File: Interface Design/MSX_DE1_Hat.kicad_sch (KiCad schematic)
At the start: 24 parts, among them J1 J1, J2 J2, J3 J3, J4 J4, J5 J5, J6 J6, U1 74LVC245A, U2 74LVC245A, U3 74LVC245A, U4 74LVC245A, U5 74LVC245A

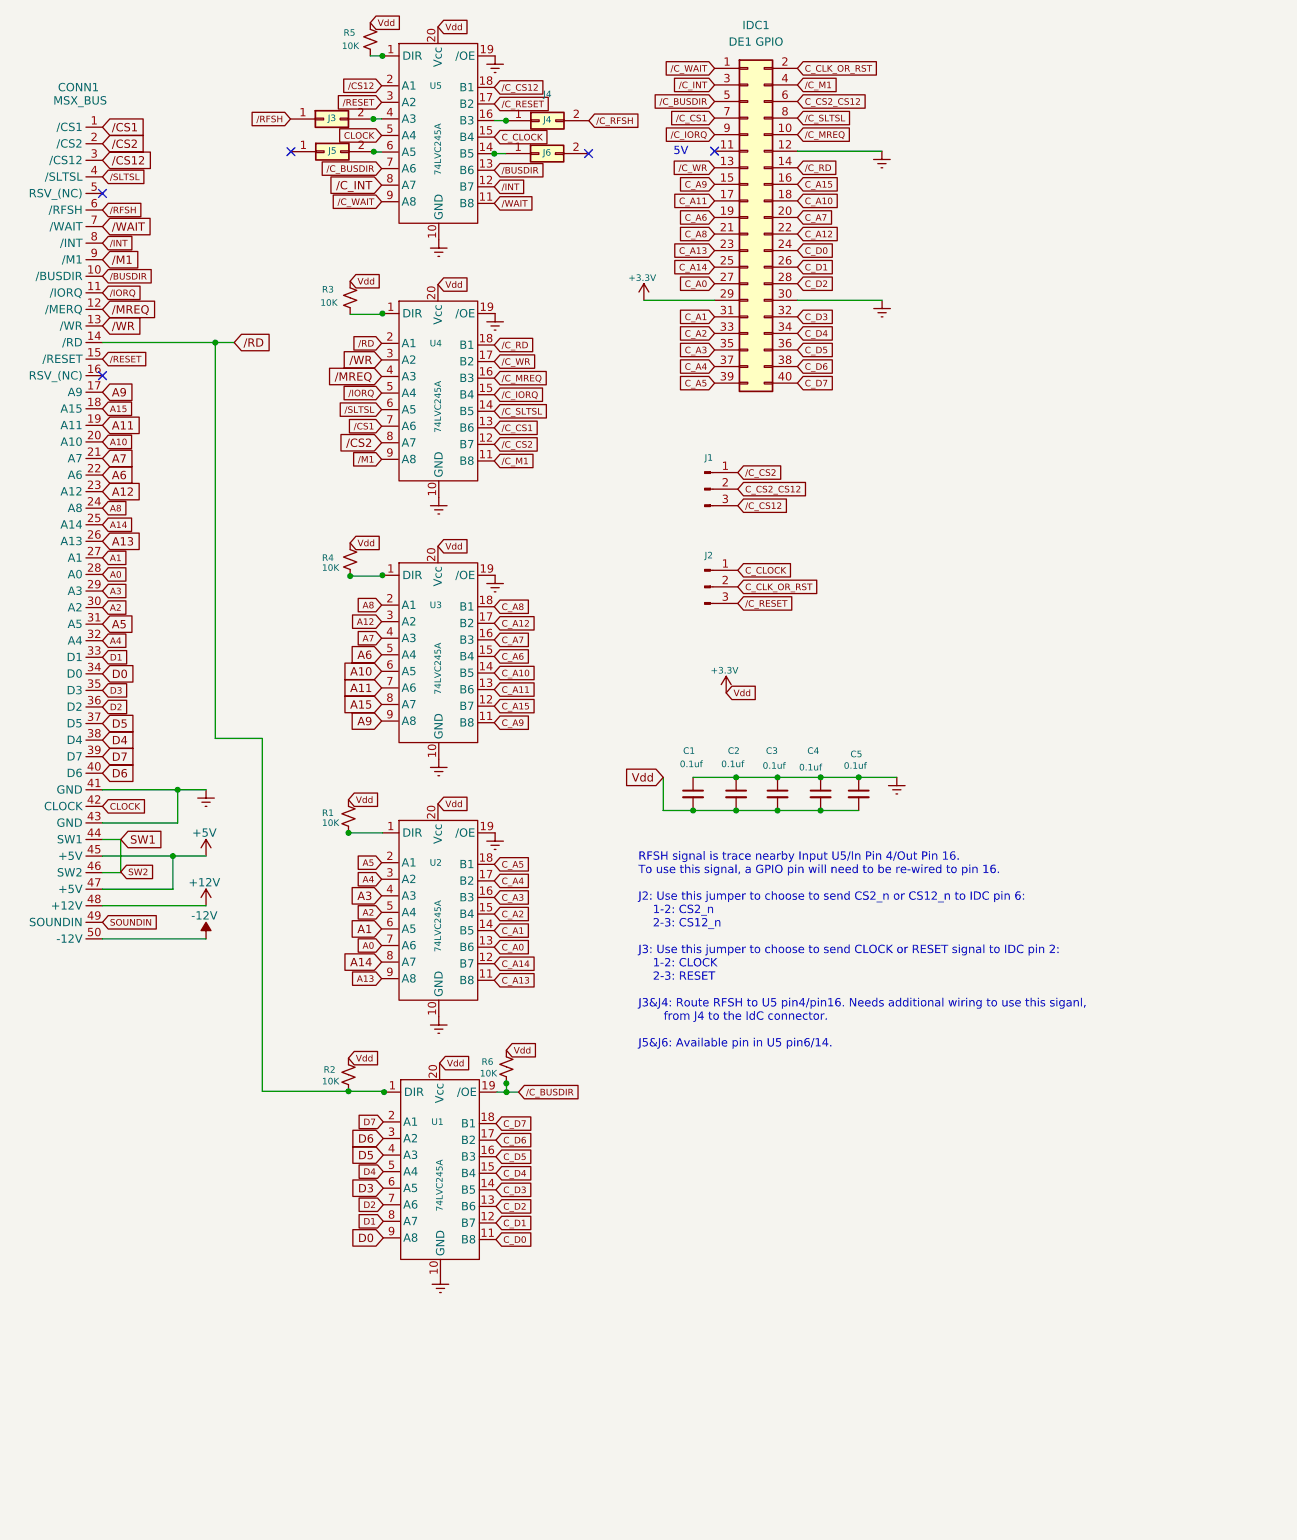
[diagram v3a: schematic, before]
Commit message: Routing new pcb for v1.1
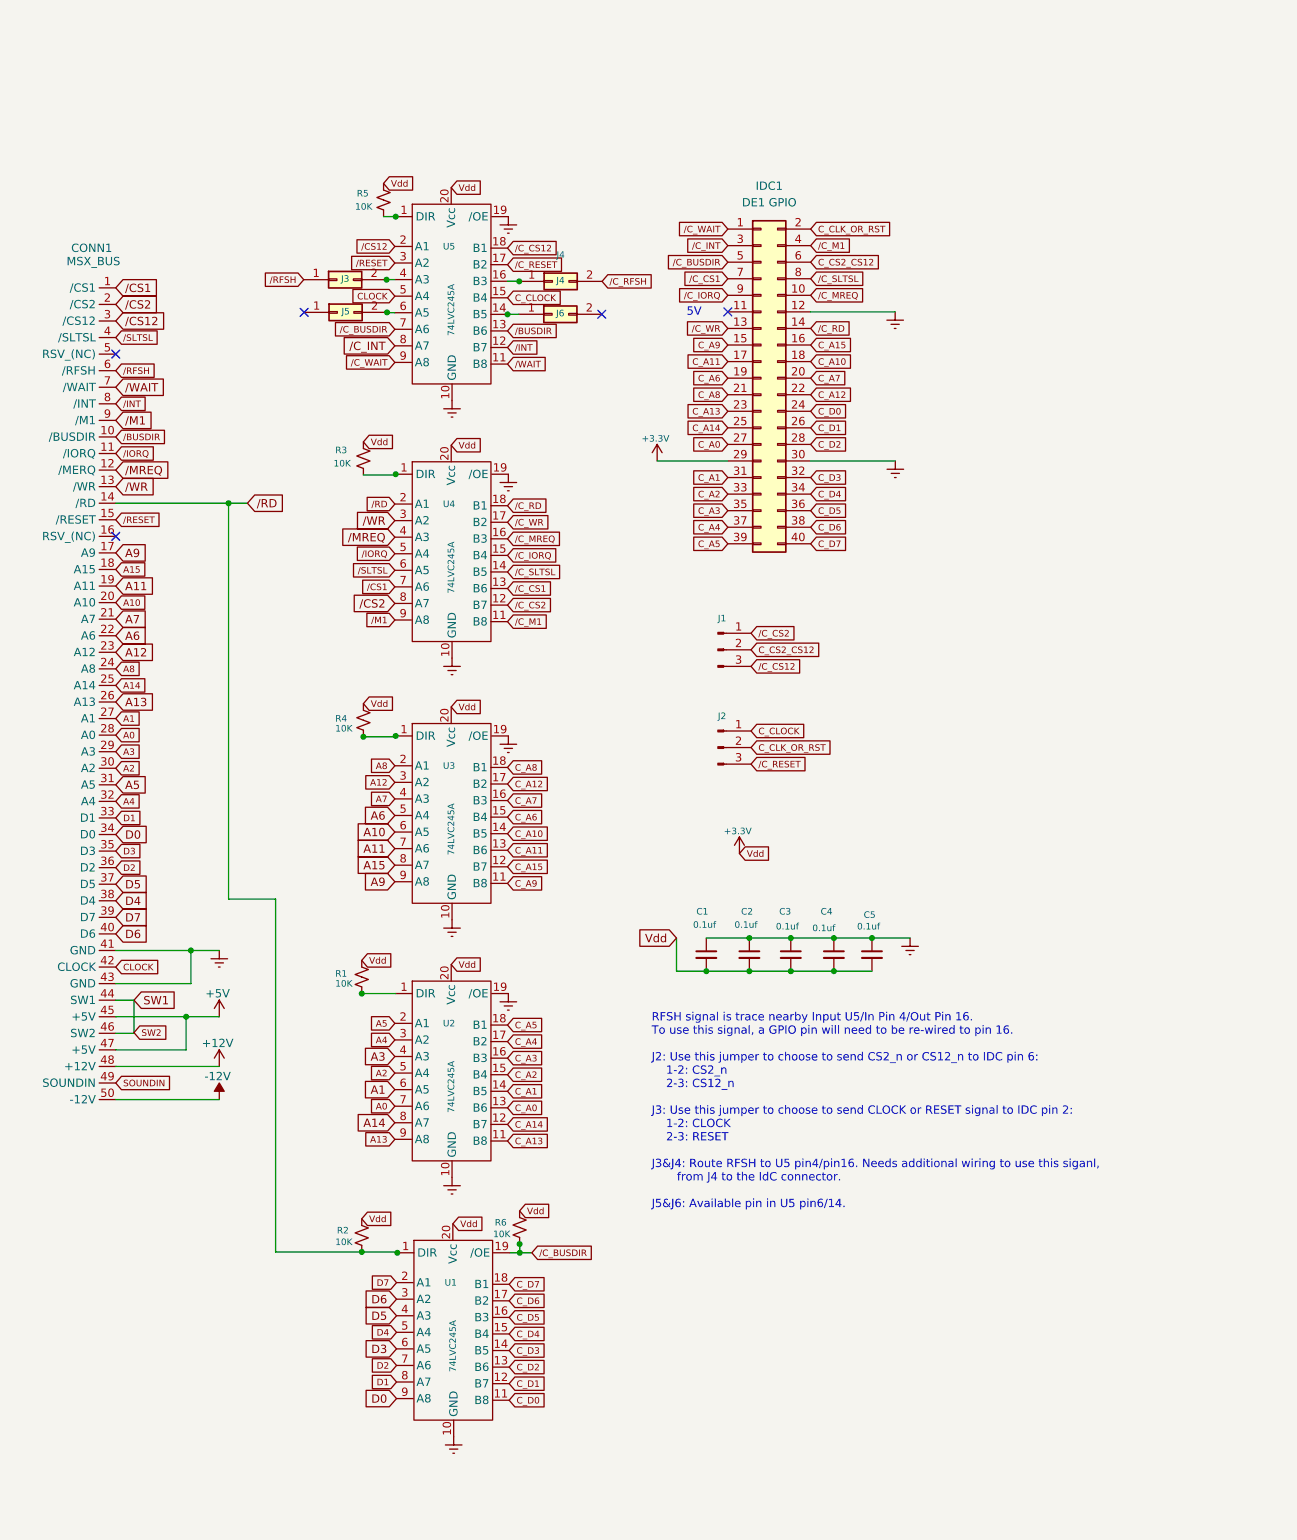
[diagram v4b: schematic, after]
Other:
- moved on the sheet: C1, C2, C3, C4, C5, CONN1, IDC1, J1, J2, J3, J4, J5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

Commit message: Fabricatin files added for the PCB v1.1
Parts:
- IDC1: footprint Connector_PinHeader_2.54mm:PinHeader_2x20_P2.54mm_Vertical -> Connector_IDC:IDC-Header_2x20_P2.54mm_Vertical
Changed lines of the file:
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@@
   (title_block
     (title "MSX DE1 Hat")
-    (date "2023-01-08")
+    (date "2023-01-09")
     (rev "1.1")
     (company "RCC")
@@
     (property "Reference" "IDC1" (id 0) (at 130.556 42.164 0))
     (property "Value" "DE1 GPIO" (id 1) (at 130.556 44.704 0))
-    (property "Footprint" "Connector_PinHeader_2.54mm:PinHeader_2x20_P2.54mm_Vertical" (id 2) (at 129.286 71.628 0)
+    (property "Footprint" "Connector_IDC:IDC-Header_2x20_P2.54mm_Vertical" (id 2) (at 129.286 71.628 0)
       (effects (font (size 1 1)) hide)
     )
@@
     )
     (path "/6f9656b3-3bfe-4b00-abcb-824b6a0202a0"
-      (reference "IDC1") (unit 1) (value "DE1 GPIO") (footprint "Connector_PinHeader_2.54mm:PinHeader_2x20_P2.54mm_Vertical")
+      (reference "IDC1") (unit 1) (value "DE1 GPIO") (footprint "Connector_IDC:IDC-Header_2x20_P2.54mm_Vertical")
     )
     (path "/4b627ac7-f426-4ad6-aa9a-a3c2759a25ab"

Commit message: Added Gerber files
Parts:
- IDC1: footprint Connector_IDC:IDC-Header_2x20_P2.54mm_Vertical -> Connector_PinHeader_2.54mm:PinHeader_2x20_P2.54mm_Vertical
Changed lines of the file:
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@@
     (property "Reference" "IDC1" (id 0) (at 130.556 42.164 0))
     (property "Value" "DE1 GPIO" (id 1) (at 130.556 44.704 0))
-    (property "Footprint" "Connector_IDC:IDC-Header_2x20_P2.54mm_Vertical" (id 2) (at 129.286 71.628 0)
+    (property "Footprint" "Connector_PinHeader_2.54mm:PinHeader_2x20_P2.54mm_Vertical" (id 2) (at 129.286 71.628 0)
       (effects (font (size 1 1)) hide)
     )
@@
     )
     (path "/6f9656b3-3bfe-4b00-abcb-824b6a0202a0"
-      (reference "IDC1") (unit 1) (value "DE1 GPIO") (footprint "Connector_IDC:IDC-Header_2x20_P2.54mm_Vertical")
+      (reference "IDC1") (unit 1) (value "DE1 GPIO") (footprint "Connector_PinHeader_2.54mm:PinHeader_2x20_P2.54mm_Vertical")
     )
     (path "/4b627ac7-f426-4ad6-aa9a-a3c2759a25ab"
